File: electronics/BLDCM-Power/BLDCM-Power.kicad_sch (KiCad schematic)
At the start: 46 parts, among them J1 501920-3001, J2 53048-0310, J3 505578-0460, J4 505578-0460, J5 FTSH-107-01-L-DV-K, J6 12402012E212A, U1 INA240A1PWR, U10 BAT54S, U11 BAT54S, U12 BAT54S, U3 TMC6300-LA, U4 INA240A1PWR, U5 TCAN1462, U6 INA240A1PWR, U7 BAT54S

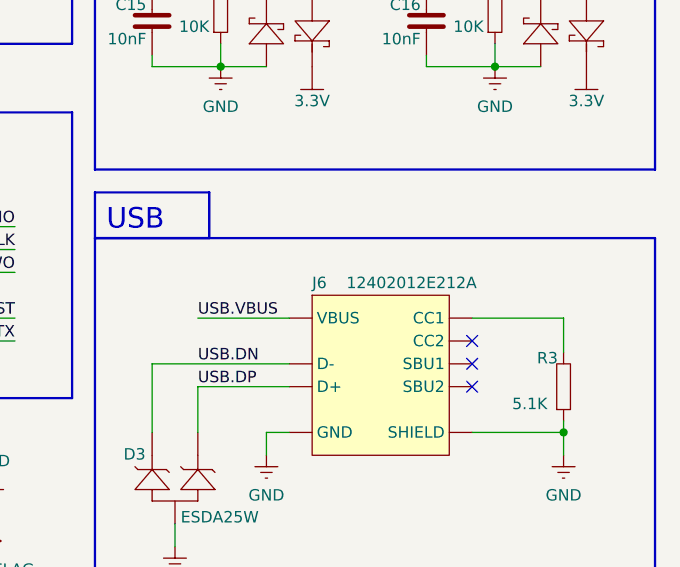
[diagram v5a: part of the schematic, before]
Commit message: Feat(pcb): Replace USB with Molex USB
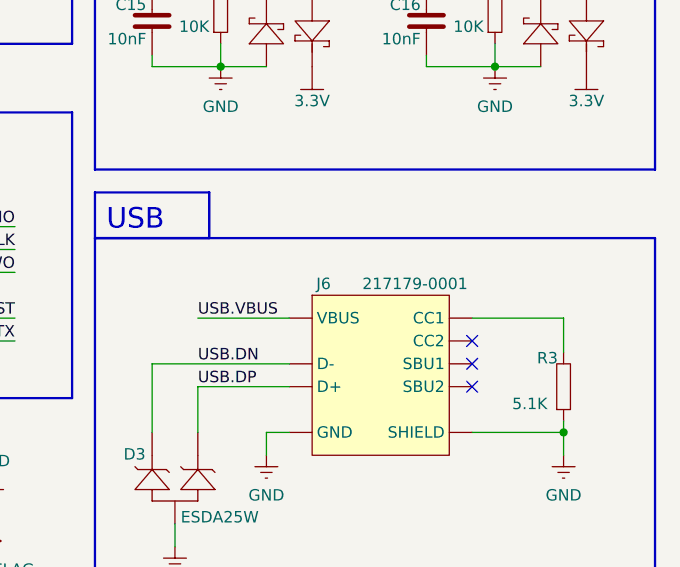
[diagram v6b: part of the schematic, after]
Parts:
- removed J6: 12402012E212A, BrenoCQ:12402012E212A, symbol BrenoCQ:USB_12402012E212A
- added J6: 217179-0001, BrenoCQ:217179-0001, symbol BrenoCQ:USB_217179-0001
- C9: footprint BrenoCQ:C_0402 -> BrenoCQ:C_0805
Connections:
- net GND: now also J6.A1_B12 (GND), J6.B1_A12 (GND), J6.SH1 (SHIELD), J6.SH2 (SHIELD), J6.SH3 (SHIELD), J6.SH4 (SHIELD)
- net USB.DN: now also J6.A7 (D-), J6.B7 (D-2)
- net USB.DP: now also J6.A6 (D+), J6.B6 (D+2)
- net VBUS: now also J6.A4_B9 (VBUS), J6.B4_A9 (VBUS)
- net at R3.2: now also J6.A5 (CC1)
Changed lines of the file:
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@@
 			)
 		)
-		(property "Footprint" "BrenoCQ:C_0402"
+		(property "Footprint" "BrenoCQ:C_0805"
 			(at 127 88.9 0)
 			(effects
@@
 	)
 	(symbol
-		(lib_id "BrenoCQ:USB_12402012E212A")
-		(at 251.46 134.62 0)
-		(unit 1)
-		(exclude_from_sim no)
-		(in_bom yes)
-		(on_board yes)
-		(dnp no)
-		(property "Reference" "J6"
-			(at 243.84 126.365 0)
-			(effects
-				(font
-					(size 1.27 1.27)
-				)
-				(justify left bottom)
-			)
-		)
-		(property "Value" "12402012E212A"
-			(at 247.65 126.365 0)
-			(effects
-				(font
-					(size 1.27 1.27)
-				)
-				(justify left bottom)
-			)
-		)
-		(property "Footprint" "BrenoCQ:12402012E212A"
-			(at 252.73 156.21 0)
-			(effects
-				(font
-					(size 1.27 1.27)
-				)
-				(hide yes)
-			)
-		)
-		(property "Datasheet" "https://cdn.amphenol-cs.com/media/wysiwyg/files/drawing/12402012-10.pdf"
-			(at 251.46 153.67 0)
-			(effects
-				(font
-					(size 1.27 1.27)
-				)
-				(hide yes)
-			)
-		)
-		(property "Description" "USB2.0, Type C, Top mount, CH 1.68mm, Dual Row SMT"
-			(at 251.46 151.13 0)
-			(effects
-				(font
-					(size 1.27 1.27)
-				)
-				(hide yes)
-			)
-		)
-		(pin "A4_B9"
-		)
-		(pin "A5"
-		)
-		(pin "A7"
-		)
-		(pin "A6"
-		)
-		(pin "A8"
-		)
-		(pin "B7"
-		)
-		(pin "SH1"
-		)
-		(pin "B4_A9"
-		)
-		(pin "SH4"
-		)
-		(pin "A1_B12"
-		)
-		(pin "B1_A12"
-		)
-		(pin "SH3"
-		)
-		(pin "B5"
-		)
-		(pin "B8"
-		)
-		(pin "B6"
-		)
-		(pin "SH2"
-		)
-		(instances
-			(project ""
-				(path "/70c0b777-4ad9-403d-bed6-4daf67ef9f8e"
-					(reference "J6")
-					(unit 1)
-				)
-			)
-		)
-	)
-	(symbol
 		(lib_id "BrenoCQ:GND")
 		(at 228.6 154.94 0)
@@
 					(unit 1)
 				)
+			)
+		)
+	)
+	(symbol
+		(lib_id "BrenoCQ:USB_217179-0001")
+		(at 251.46 134.62 0)
+		(unit 1)
+		(exclude_from_sim no)
+		(in_bom yes)
+		(on_board yes)
+		(dnp no)
+		(property "Reference" "J6"
+			(at 245.11 125.73 0)
+			(effects
+				(font
+					(size 1.27 1.27)
+				)
+			)
+		)
+		(property "Value" "217179-0001"
+			(at 255.27 125.73 0)
+			(effects
+				(font
+					(size 1.27 1.27)
+				)
+			)
+		)
+		(property "Footprint" "BrenoCQ:217179-0001"
+			(at 252.73 151.765 0)
+			(effects
+				(font
+					(size 1.27 1.27)
+				)
+				(hide yes)
+			)
+		)
+		(property "Datasheet" "https://www.molex.com/content/dam/molex/molex-dot-com/products/automated/en-us/salesdrawingpdf/217/217179/2171790001_sd.pdf"
+			(at 251.46 149.225 0)
+			(effects
+				(font
+					(size 1.27 1.27)
+				)
+				(hide yes)
+			)
+		)
+		(property "Description" "USB2.0, Type C, Molex, Top mount, Dual Row SMT, 16Ckt"
+			(at 251.46 146.685 0)
+			(effects
+				(font
+					(size 1.27 1.27)
+				)
+				(hide yes)
+			)
+		)
+		(pin "A8"
+		)
+		(pin "B1_A12"
+		)
+		(pin "SH3"
+		)
+		(pin "B4_A9"
+		)
+		(pin "B7"
+		)
+		(pin "A6"
+		)
+		(pin "SH2"
+		)
+		(pin "A1_B12"
+		)
+		(pin "B6"
+		)
+		(pin "A4_B9"
+		)
+		(pin "SH1"
+		)
+		(pin "A7"
+		)
+		(pin "SH4"
+		)
+		(pin "A5"
+		)
+		(pin "B5"
+		)
+		(pin "B8"
+		)
+		(instances
+			(project ""
+				(path "/70c0b777-4ad9-403d-bed6-4daf67ef9f8e"
+					(reference "J6")
+					(unit 1)
+				)

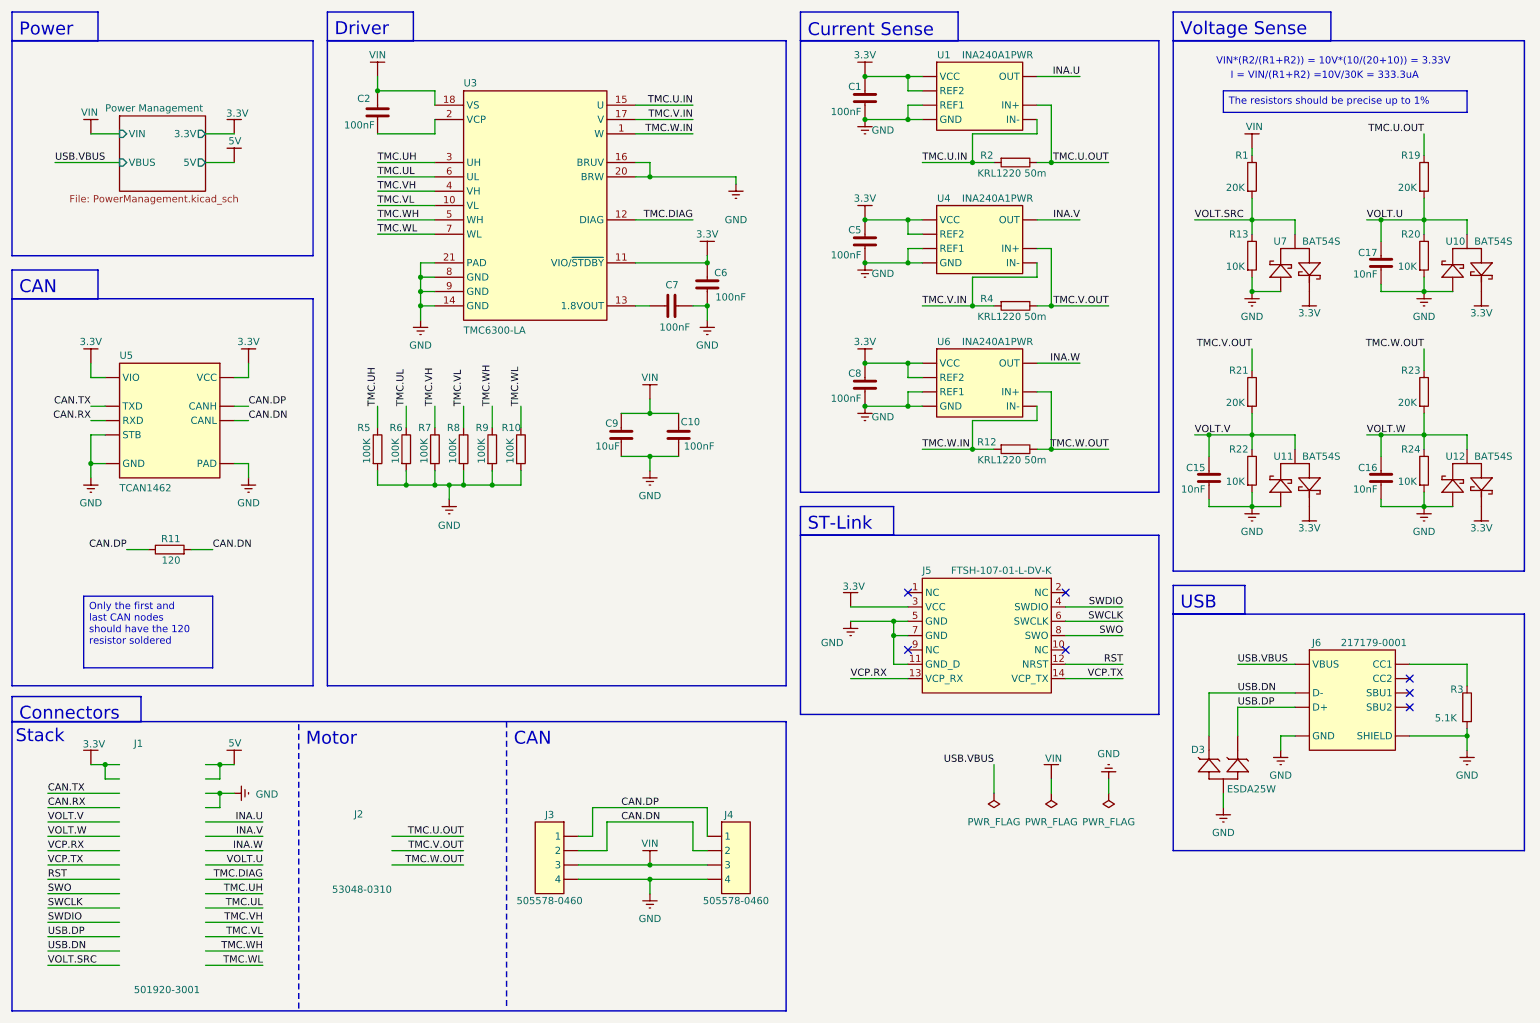
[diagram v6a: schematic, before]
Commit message: Refactor(schematic): Rename INA nets to CURR
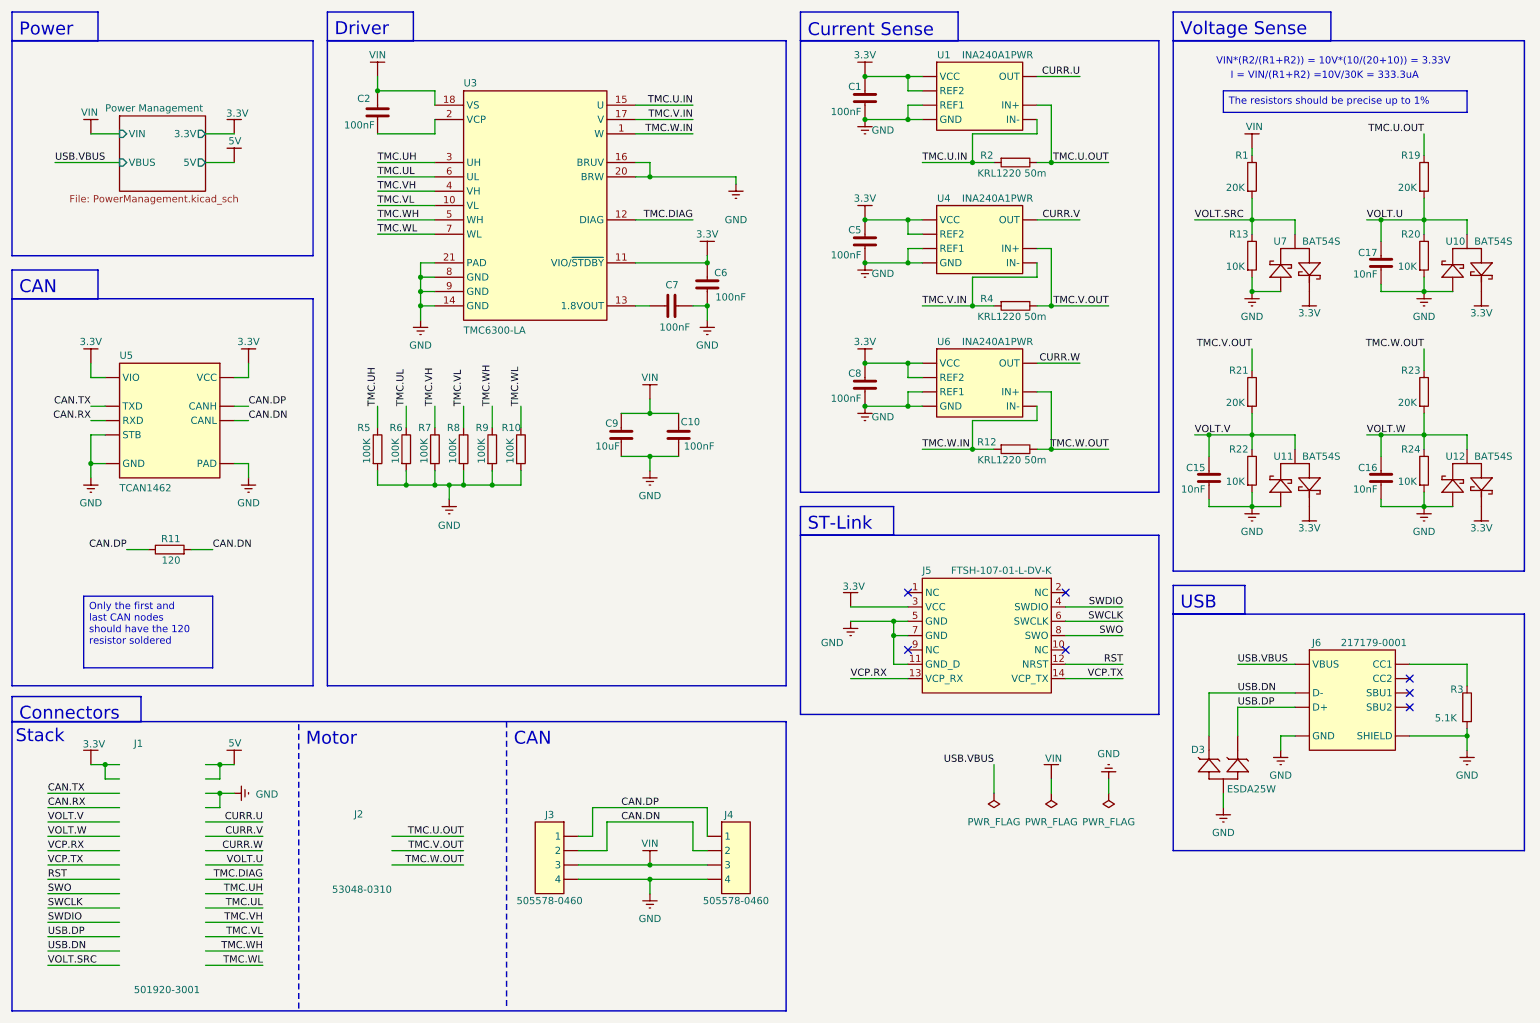
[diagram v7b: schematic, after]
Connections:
- net INA.U renamed CURR.U
- net INA.V renamed CURR.V
- net INA.W renamed CURR.W
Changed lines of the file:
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@@
 		)
 	)
-	(label "INA.U"
+	(label "CURR.U"
 		(at 203.2 25.4 180)
 		(effects
@@
 		)
 	)
-	(label "INA.U"
+	(label "CURR.U"
 		(at 58.42 157.48 180)
 		(effects
@@
 		)
 	)
-	(label "INA.V"
+	(label "CURR.V"
 		(at 58.42 160.02 180)
 		(effects
@@
 		)
 	)
-	(label "INA.W"
+	(label "CURR.W"
 		(at 58.42 162.56 180)
 		(effects
@@
 		)
 	)
-	(label "INA.V"
+	(label "CURR.V"
 		(at 203.2 50.8 180)
 		(effects
@@
 		)
 	)
-	(label "INA.W"
+	(label "CURR.W"
 		(at 203.2 76.2 180)
 		(effects

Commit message: Feat: Add schematic PDFs for v1.0 PCBs
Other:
- company: (none) -> Breno Cunha Queiroz
- title: (none) -> BLDCM Power
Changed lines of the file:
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@@
 	(paper "A4")
 	(title_block
-		(date "2025-05-06")
-		(rev "v3")
+		(title "BLDCM Power")
+		(date "2025-07-19")
+		(rev "v1.0")
+		(company "Breno Cunha Queiroz")
 	)
 	(rectangle
